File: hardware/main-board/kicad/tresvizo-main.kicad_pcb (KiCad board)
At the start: 4 copper layers, 46 x 64 mm, 121 parts, among them J101 PANEL_USB, J102 BATTERY, J301 GNSS, J401 TF-015, J402 BOTON, J403 OLED, J404 NTC, J405 IMU, J406 LEDS, Q101 AO3400A, Q102 AO3401A, Q103 AO3400A, Q401 AO3401A, Q402 AO3400A, SW201 RESET, SW202 BOOT, U101 USBLC6-2SC6, U102 BQ25798RQMR, U103 MAX17048G+T10, U105 TPS62903RPJR, U201 ESP32-S3-MINI-1-N4R2, U301 TPS63070RNMR, U302 USBLC6-2SC6, U303 USBLC6-2SC6

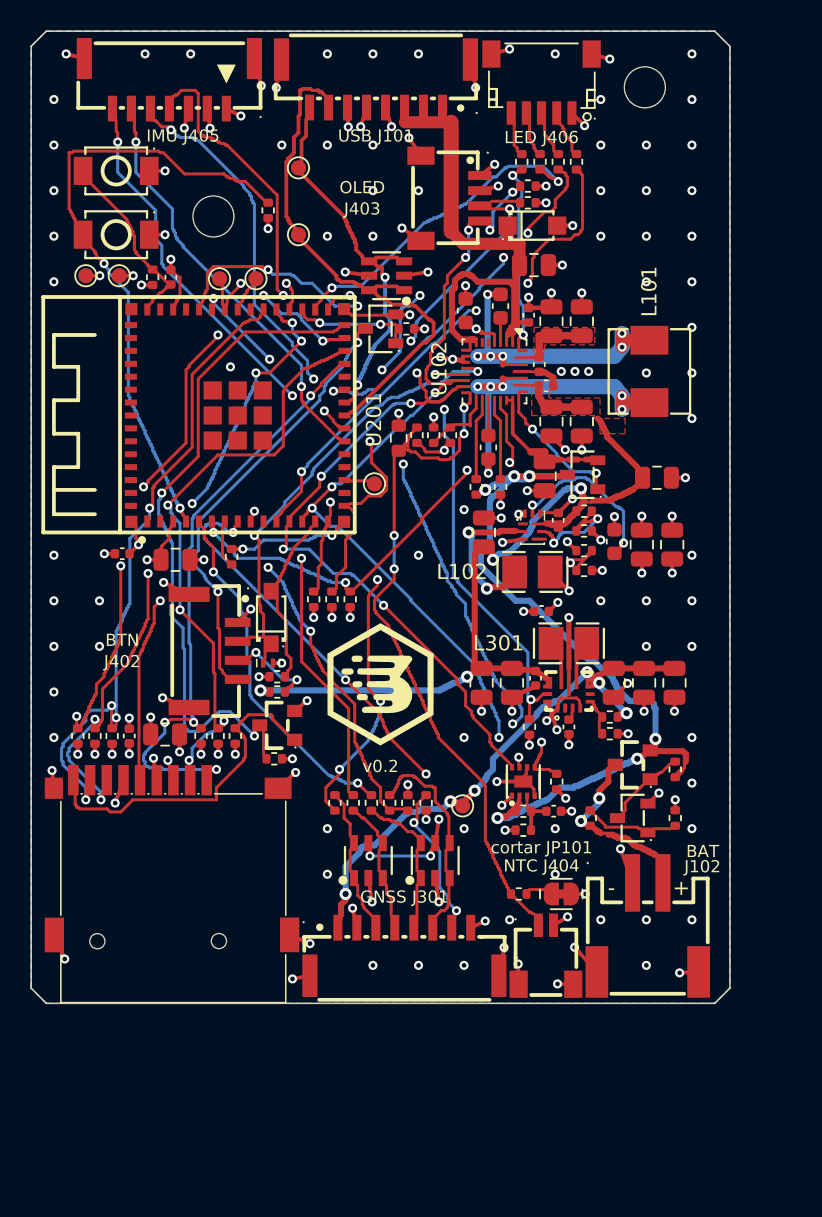
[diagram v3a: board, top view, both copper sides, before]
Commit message: Placa principal v0.2: ESP32-S3-WROOM-1-N16R2 en lugar del MINI-1 y sin LEDs del panel
- U201 = ESP32-S3-WROOM-1-N16R2 (C2913205): 16 MB de flash y 2 MB de PSRAM quad. Huella y
  modelos de LCSC; el .step se corrió 3.65 mm para que coincida con su .wrl y la huella.
- GPIO nuevos para rutear el módulo en la misma placa: microSD CLK 6, CMD 7, D0 5, D1 4, D2 16,
  D3 15 y detección 17; UART del GNSS TX 8 / RX 9; PPS 10, EVENT 11, RESET 12; I2C 13/14;
  IMU 41/42 con INT1 2 e INT3 1; botón 18; puntos de prueba en 35, 36 y 37. README y pinout
  con el mapa para el firmware.
- Fuera J406, sus resistencias y la del STAT del cargador: la carcasa V2.3 no lleva LEDs.
- Misma placa de 46 x 64 mm. H1 pasa a (12.0, 9.6) y el corte del riel +X frente a la antena a
  v 15.1-34.0; antena sin cobre en u 0-6.7, v 15.7-33.7.
- R108 sale de debajo de los pines de la microSD (el ruteador se ciclaba entre SD_D3 y
  CHG_INT_N) y el divisor de TS va bajo L102.
- BUCK_SW y el PGND de U105 prerruteados: la vía que el ruteador ponía junto a L102 hacía caer
  el relleno de zonas de KiCad 10 (-11, también en kicad-cli). route_rest guarda las pistas que
  arranca mientras dura el ruteo.
- DRC 0, sin conexiones pendientes y con paridad en la placa y en el panel; ERC 0. Costo
  estimado 206.86 USD por 5 juegos (montaje + piezas, sin PCB).
- Carcasa V2.3: H1 en z 77.9, riel +X cortado en z 53.7-72.4, placa superior recortada frente
  a la antena y SMA de la carrier con las medidas de la foto. Placa nueva contra la carcasa:
  0 mm3 de choques.
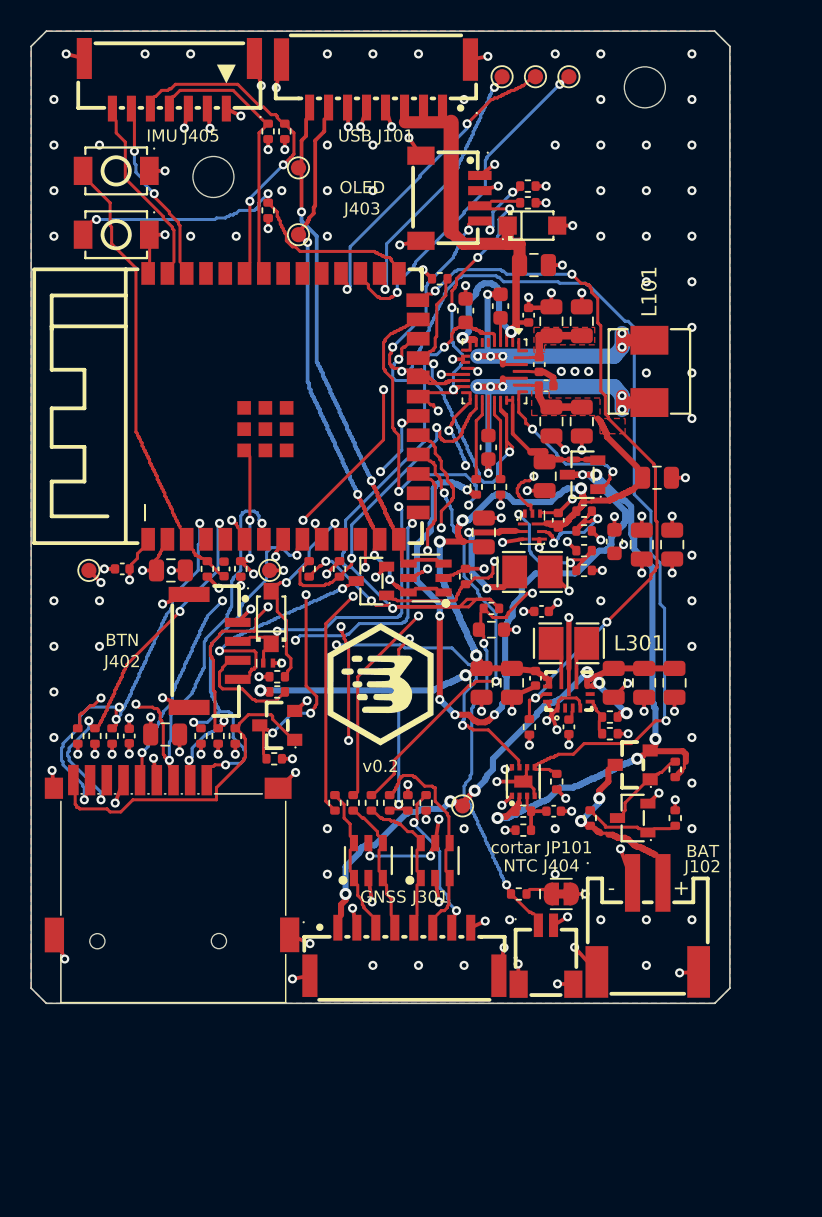
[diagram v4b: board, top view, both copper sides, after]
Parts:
- removed J406: LEDS, tresvizo_lcsc:CONN-SMD_SM05B-SRSS-TB-LF-SN
- removed R119: 22k, Resistor_SMD:R_0402_1005Metric
- removed R413: 100k, Resistor_SMD:R_0402_1005Metric
- removed R414, R415: 4.7k, Resistor_SMD:R_0402_1005Metric
- R109: value 1k -> 1M
- R110: value 1M -> 100k
- R111: value 100k -> 1M
- R112: value 1M -> 0
- R113: value 0 -> 10k
- R114: value 10k -> 0
- R115: value 0 -> 22k
- R116: value 22k -> 10k
- R117: value 10k -> 100k
- R118: value 100k -> 22k
- R409: value 1k -> 100
- R410: value 100 -> 100k
- R411, R412: value 100 -> 4.7k
- TP203: value IO14 -> IO35
- TP204: value IO42 -> IO36
- TP205: value TXD0 -> IO37
- U201: value ESP32-S3-MINI-1-N4R2 -> ESP32-S3-WROOM-1-N16R2; footprint tresvizo_lcsc:BULETM-SMD_ESP32-S3-MINI-1-N8 -> tresvizo_lcsc:WIRELM-SMD_ESP32-S3-WROOM-1
- moved R109 41.3 mm to (142.4, 148.6)
- moved R409 40.1 mm to (116.2, 143.5), turned to 0 degrees
- moved R412 36.9 mm to (116.7, 106.6), turned to 90 degrees
- moved TP203 28.1 mm to (131.0, 103.0)
- moved R410 28.0 mm to (128.6, 135.9)
- moved TP205 24.7 mm to (133.2, 103.0)
- moved TP204 24.5 mm to (135.4, 103.0)
- moved R108 21.9 mm to (126.9, 116.3), turned to 0 degrees
- moved TP202 21.8 mm to (115.7, 135.5)
- moved R115 21.4 mm to (136.4, 131.6)
- moved U101 20.1 mm to (126.0, 136.0)
- moved R201 19.5 mm to (111.6, 135.4)
- moved C203 19.5 mm to (112.7, 135.4)
- moved TP201 19.4 mm to (103.8, 135.5)
- moved R411 18.0 mm to (115.6, 106.6)
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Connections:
- R109 pad 1: /Alimentación, carga y batería/CHG_STAT -> /Alimentación, carga y batería/VPACK
- R109 pad 2: CHG_LED_K -> /Alimentación, carga y batería/BATREV_G
- R110 pad 1: /Alimentación, carga y batería/VPACK -> /Alimentación, carga y batería/VBATT_IN
- R110 pad 2: /Alimentación, carga y batería/BATREV_G -> /Alimentación, carga y batería/BATREV_SENSE
- R111 pad 1: /Alimentación, carga y batería/VBATT_IN -> /Alimentación, carga y batería/BATREV_SENSE
- R111 pad 2: /Alimentación, carga y batería/BATREV_SENSE -> GND
- R112 pad 1: /Alimentación, carga y batería/BATREV_SENSE -> /Alimentación, carga y batería/VPACK
- R112 pad 2: GND -> /Alimentación, carga y batería/FG_VDD
- R113 pad 1: /Alimentación, carga y batería/VPACK -> +3V3
- R113 pad 2: /Alimentación, carga y batería/FG_VDD -> FG_ALRT_N
- R114 pad 2: FG_ALRT_N -> /Alimentación, carga y batería/FG_VDD
- R115 pad 1: +3V3 -> VSYS
- R115 pad 2: /Alimentación, carga y batería/FG_VDD -> /Alimentación, carga y batería/BUCK_EN
- R116 pad 1: VSYS -> /Alimentación, carga y batería/BUCK_EN
- R116 pad 2: /Alimentación, carga y batería/BUCK_EN -> GND
- R117 pad 1: /Alimentación, carga y batería/BUCK_EN -> +3V3
- R117 pad 2: GND -> /Alimentación, carga y batería/BUCK_FB
- R118 pad 1: +3V3 -> /Alimentación, carga y batería/BUCK_FB
- R118 pad 2: /Alimentación, carga y batería/BUCK_FB -> GND
- R304 pad 1: ESP_TX0 -> GNSS_TX_MCU
- R409 pad 1: LED_R -> VSYS
- R409 pad 2: /microSD, IMU por conector y panel/LED_R_K -> /microSD, IMU por conector y panel/BTN_LED_A
- R410 pad 1: LED_G -> BTN_LED_EN
- R410 pad 2: /microSD, IMU por conector y panel/LED_G_K -> GND
- R411 pad 1: LED_B -> +3V3
- R411 pad 2: /microSD, IMU por conector y panel/LED_B_K -> IMU_SDA
- R412 pad 1: VSYS -> +3V3
- R412 pad 2: /microSD, IMU por conector y panel/BTN_LED_A -> IMU_SCL
- TP203 pad 1: /ESP32-S3/ESP_IO14 -> /ESP32-S3/ESP_IO35
- TP204 pad 1: /ESP32-S3/ESP_IO42 -> /ESP32-S3/ESP_IO36
- TP205 pad 1: ESP_TX0 -> /ESP32-S3/ESP_IO37
- U102 pad 1: /Alimentación, carga y batería/CHG_STAT -> unconnected-(U102-STAT-Pad1)
- U201 pad 10: unconnected-(U201-IO6-Pad10) -> SD_DET
- U201 pad 11: LED_R -> BTN_SENSE_N
- U201 pad 12: I2C_SDA -> GNSS_TX_MCU
- U201 pad 13: I2C_SCL -> USB_DN
- U201 pad 14: BTN_SENSE_N -> USB_DP
- U201 pad 15: IMU_SDA -> /ESP32-S3/ESP_IO3
- U201 pad 16: IMU_SCL -> unconnected-(U201-IO46-Pad16)
- U201 pad 17: unconnected-(U201-IO13-Pad17) -> GNSS_TXD2_MCU
- U201 pad 18: /ESP32-S3/ESP_IO14 -> GNSS_PPS_MCU
- U201 pad 19: unconnected-(U201-IO15-Pad19) -> GNSS_EVENT_MCU
- U201 pad 2: GND -> +3V3
- U201 pad 20: unconnected-(U201-IO16-Pad20) -> GNSS_RESET_MCU
- U201 pad 21: IMU_INT1 -> I2C_SDA
- U201 pad 22: IMU_INT3 -> I2C_SCL
- U201 pad 23: USB_DN -> CHG_INT_N
- U201 pad 24: USB_DP -> FG_ALRT_N
- U201 pad 25: LED_G -> BTN_LED_EN
- U201 pad 26: unconnected-(U201-IO26-Pad26) -> GNSS_PWR_EN
- U201 pad 27: SD_D2 -> /ESP32-S3/ESP_BOOT
- U201 pad 28: SD_D3 -> /ESP32-S3/ESP_IO35
- U201 pad 29: SD_CMD -> /ESP32-S3/ESP_IO36
- U201 pad 3: +3V3 -> /ESP32-S3/ESP_EN
- U201 pad 30: SD_DET -> /ESP32-S3/ESP_IO37
- U201 pad 31: FG_ALRT_N -> unconnected-(U201-IO38-Pad31)
- U201 pad 32: LED_B -> unconnected-(U201-IO39-Pad32)
- U201 pad 33: BTN_LED_EN -> unconnected-(U201-IO40-Pad33)
- U201 pad 34: SD_CLK -> IMU_SDA
- U201 pad 35: SD_D0 -> IMU_SCL
- U201 pad 36: SD_D1 -> unconnected-(U201-RXD0-Pad36)
- U201 pad 38: /ESP32-S3/ESP_IO42 -> IMU_INT1
- U201 pad 39: ESP_TX0 -> IMU_INT3
- U201 pad 4: /ESP32-S3/ESP_BOOT -> SD_D1
- U201 pad 40: GNSS_TXD2_MCU -> GND
- U201 pad 41: GNSS_PWR_EN -> GND
- U201 pad 5: GNSS_PPS_MCU -> SD_D0
- U201 pad 6: CHG_INT_N -> SD_CLK
- U201 pad 7: /ESP32-S3/ESP_IO3 -> SD_CMD
- U201 pad 8: GNSS_RESET_MCU -> SD_D3
- U201 pad 9: GNSS_EVENT_MCU -> SD_D2
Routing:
- net ESP_TX0: track 46.9 -> 0.00 mm, vias 4 -> 0
- net /Alimentación, carga y batería/REGN: track 15.4 -> 49.6 mm, vias 2 -> 4
- net LED_R: track 33.7 -> 0.00 mm, vias 3 -> 0
- net /Alimentación, carga y batería/VPACK: track 53.3 -> 86.6 mm, vias 6 -> 10
- net BTN_LED_EN: track 7.38 -> 33.8 mm, vias 2 -> 3
- net SD_DET: track 43.9 -> 19.0 mm, vias 2 -> 4
- net LED_G: track 23.5 -> 0.00 mm, vias 3 -> 0
- net IMU_SDA: track 38.2 -> 16.1 mm, vias 2 -> 0
- net LED_B: track 21.3 -> 0.00 mm, vias 2 -> 0
- net /ESP32-S3/ESP_IO36: track 0.00 -> 21.2 mm, vias 0 -> 2
- net IMU_SCL: track 40.3 -> 20.0 mm, vias 3 -> 2
- net /ESP32-S3/ESP_IO37: track 0.00 -> 19.9 mm, vias 0 -> 2
- net /ESP32-S3/ESP_IO3: track 2.47 -> 21.2 mm, vias 0 -> 3
- net GNSS_TX_MCU: track 0.00 -> 18.2 mm, vias 0 -> 2
- net SD_D0: track 42.5 -> 24.2 mm, vias 7 -> 4
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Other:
- board text added: "1S: R103=4.7k R116=10k U103=MAX17048"
- board text added: "2S: R103=8.2k R116=3.9k U103=MAX17049 R112 NC R114 0R"
- board text removed: "1S: R103=4.7k R117=10k U103=MAX17048"
- board text removed: "2S: R103=8.2k R117=3.9k U103=MAX17049 R113 NC R115 0R"
- board text removed: "LED J406"
